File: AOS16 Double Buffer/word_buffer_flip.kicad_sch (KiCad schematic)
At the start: 5 parts, among them IC4 SN74LVC16245ADGVR

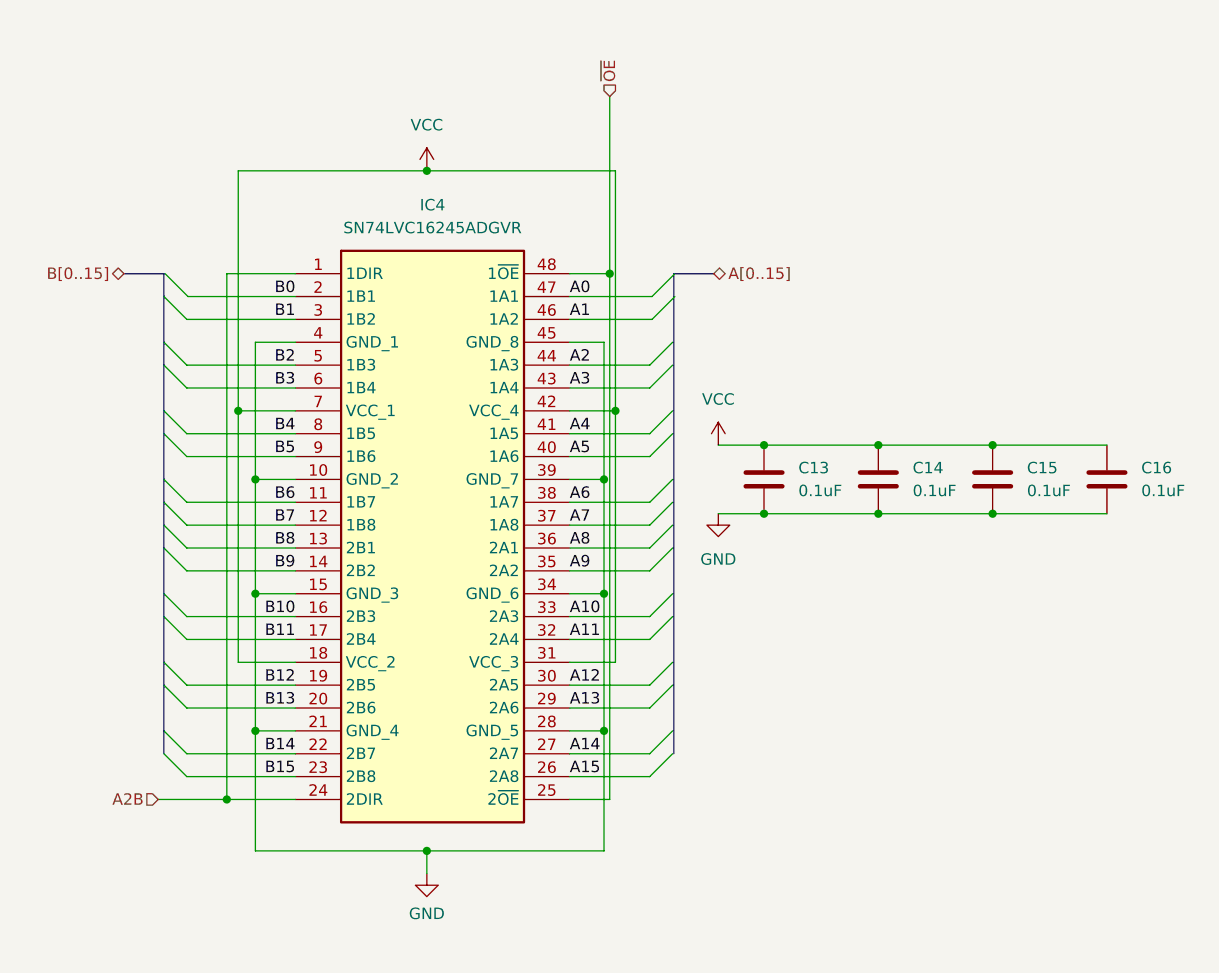
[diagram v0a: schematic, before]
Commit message: updated double buffer
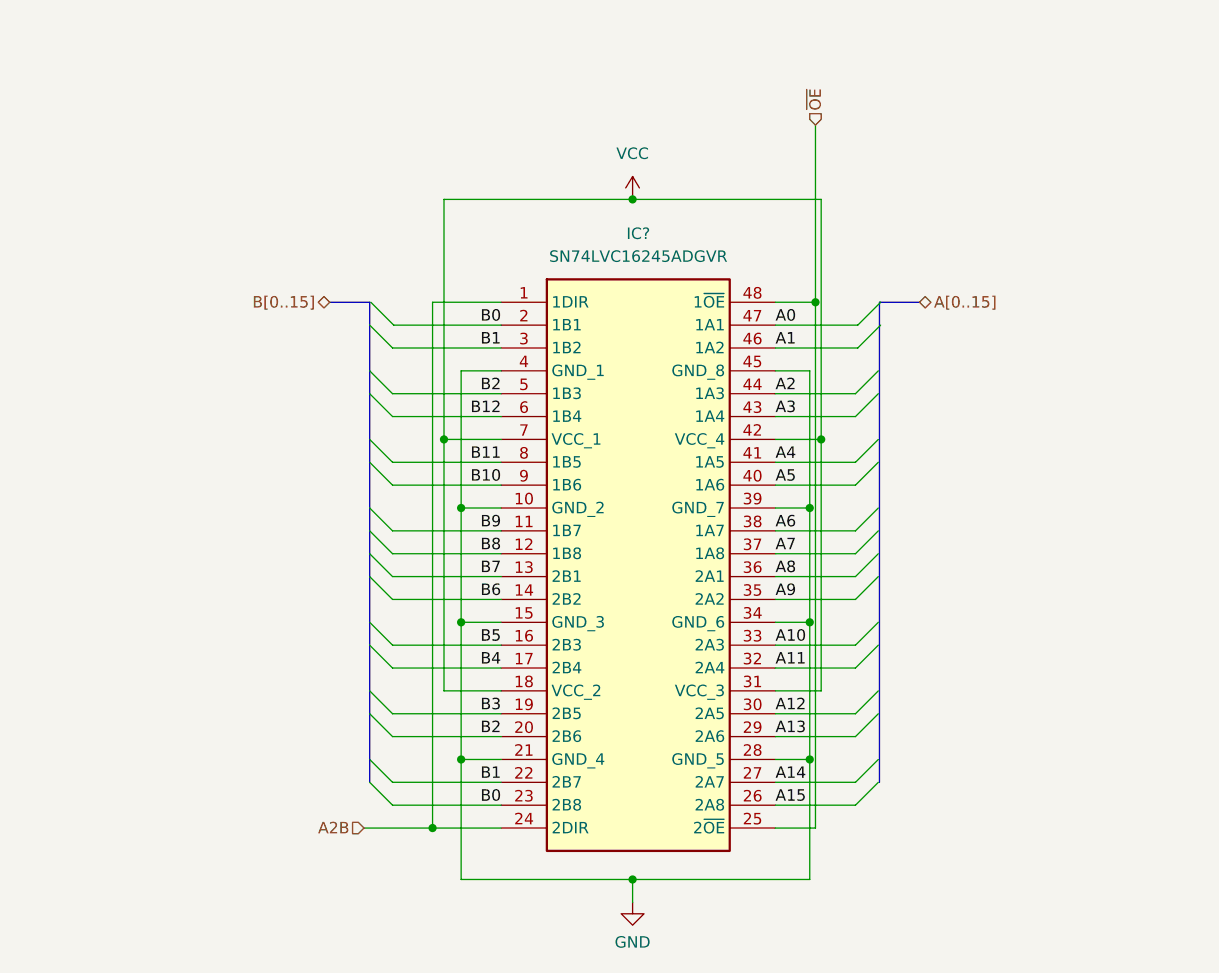
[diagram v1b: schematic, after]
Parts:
- removed C13, C14, C15, C16: 0.1uF, Capacitor_SMD:C_0603_1608Metric, symbol Device:C
- removed IC4: SN74LVC16245ADGVR, sn74lvc:SOP40P640X120-48N, symbol SN74LVC16245ADGVR:SN74LVC16245ADGVR
- added IC?: SN74LVC16245ADGVR, sn74lvc:SOP40P640X120-48N, symbol SN74LVC16245ADGVR:SN74LVC16245ADGVR
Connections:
- net A0: now also IC?.47 (1A1)
- net A1: now also IC?.46 (1A2)
- net A10: now also IC?.33 (2A3)
- net A11: now also IC?.32 (2A4)
- net A12: now also IC?.30 (2A5)
- net A13: now also IC?.29 (2A6)
- net A14: now also IC?.27 (2A7)
- net A15: now also IC?.26 (2A8)
- net A2: now also IC?.44 (1A3)
- net A2B: now also IC?.1 (1DIR), IC?.24 (2DIR)
- net A3: now also IC?.43 (1A4)
- net A4: now also IC?.41 (1A5)
- net A5: now also IC?.40 (1A6)
- net A6: now also IC?.38 (1A7)
- net A7: now also IC?.37 (1A8)
- net A8: now also IC?.36 (2A1)
- net A9: now also IC?.35 (2A2)
- net B0: now also IC?.2 (1B1), IC?.23 (2B8)
- net B1: now also IC?.22 (2B7), IC?.3 (1B2)
- net B10: now also IC?.9 (1B6)
- net B11: now also IC?.8 (1B5)
- net B12: now also IC?.6 (1B4)
- net B2: now also IC?.20 (2B6), IC?.5 (1B3)
- net B3: now also IC?.19 (2B5)
- net B4: now also IC?.17 (2B4)
- net B5: now also IC?.16 (2B3)
- net B6: now also IC?.14 (2B2)
- net B7: now also IC?.13 (2B1)
- net B8: now also IC?.12 (1B8)
- net B9: now also IC?.11 (1B7)
- net GND: now also IC?.10 (GND_2), IC?.15 (GND_3), IC?.21 (GND_4), IC?.28 (GND_5), IC?.34 (GND_6), IC?.39 (GND_7), IC?.4 (GND_1), IC?.45 (GND_8)
- net VCC: now also IC?.18 (VCC_2), IC?.31 (VCC_3), IC?.42 (VCC_4), IC?.7 (VCC_1)
- net ~{OE}: now also IC?.25 (2~{OE}), IC?.48 (1~{OE})
